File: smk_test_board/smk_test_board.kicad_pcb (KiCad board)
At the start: 2 copper layers, 76 x 113.2 mm, 46 parts, among them J1 Battery JST-SH, SW00 KS-2P02B01-02, SW01 KS-2P02B01-02, SW10 KS-2P02B01-02, SW11 KS-2P02B01-02, SW12 KS-2P02B01-02, SW20 KS-2P02B01-02, SW21 KS-2P02B01-02, SW22 KS-2P02B01-02, U1 XIAO_ESP32C6, U2 SN74AHCT1G125DBVR

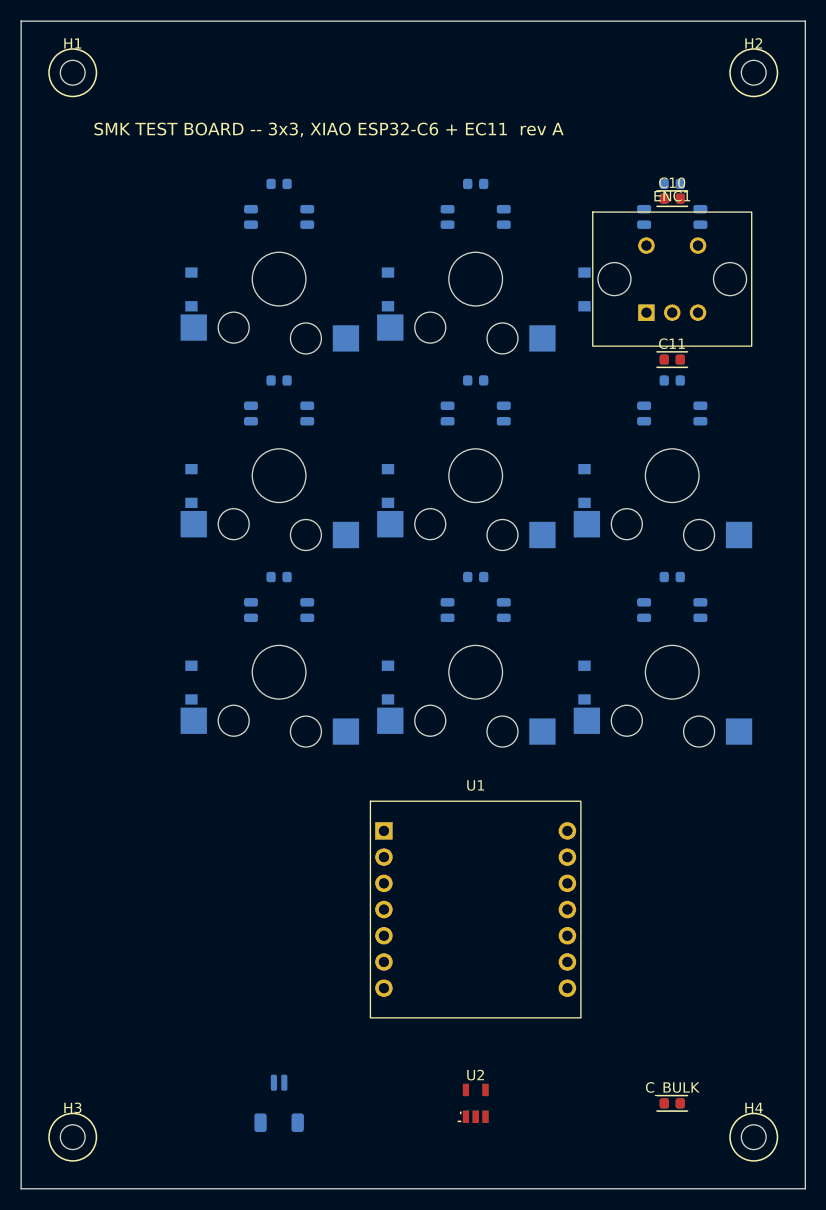
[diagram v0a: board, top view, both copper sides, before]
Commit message: Mill the SK6812MINI-E light windows into all nine LEDs
_fp_sk6812mini_tb() re-rendered the SK6812MINI-E footprint inline and
emitted 4 pads, 5 B.SilkS lines, a B.CrtYd rect, 2 B.Fab items and the
3D model -- then stopped. The library master
smk_test_board.pretty/SK6812MINI_E.kicad_mod additionally carries 20
Edge.Cuts primitives (8 fp_line + 12 fp_arc) forming the ~3.4 x 3.0mm
rounded-rect cutout, plus the pin-1 silk polarity triangle. None of that
was emitted.

These are REVERSE-MOUNT LEDs on the back of the board, shining forward
through it into each switch's north window. With no milled openings they
do nothing at all, and it cannot be reworked after fabrication.

  grep -c Edge.Cuts  smk_test_board/smk_test_board.kicad_pcb : 2  ->  182
  (1 layer declaration + 1 board outline + 9 LEDs x 20 primitives)
  Library master: 20. Proven sibling smk_kbd_rp2040 (58 LEDs): 1182.

The geometry is transcribed from the library master, not re-derived, and
cross-checked against how the sibling board actually stores its own 58
SK6812MINI_E instances: identical local numbers, footprint (at ... 180).
Footprint graphics live in footprint-LOCAL coordinates in both .kicad_mod
and .kicad_pcb -- KiCad applies each instance's own (at x y rot) -- so one
local copy lands correctly rotated at all nine placed positions.

The comment above these re-renders claimed they matched the library
master "byte-for-byte". They never did (the masters spell rectangles as
four fp_lines where gm.fprect() emits one fp_rect, and every uuid
differs), and that unfalsifiable-sounding claim is what let a dropped
layer survive review. Replaced with what is actually guaranteed --
equivalent geometry, per element-class -- and made checkable:

  test_inline_rerenders_match_their_library_master compares every inline
  re-render against its master by element-class (pads / silk / courtyard /
  fab / Edge.Cuts / text / model), normalising only the differences that
  are genuinely spelling and not geometry (fp_rect vs 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
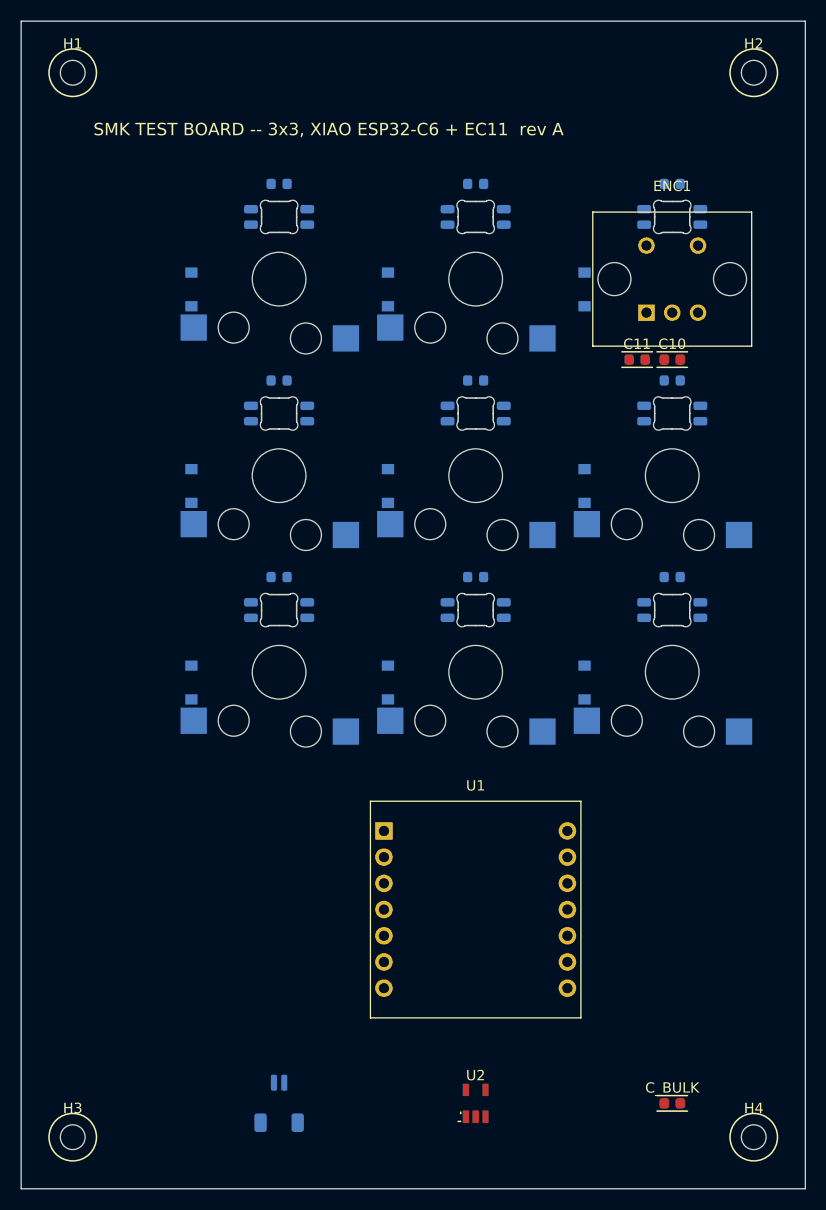
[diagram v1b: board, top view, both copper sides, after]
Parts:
- moved C10 15.6 mm to (63.1, 32.8)
- moved C11 3.40 mm to (59.7, 32.8)

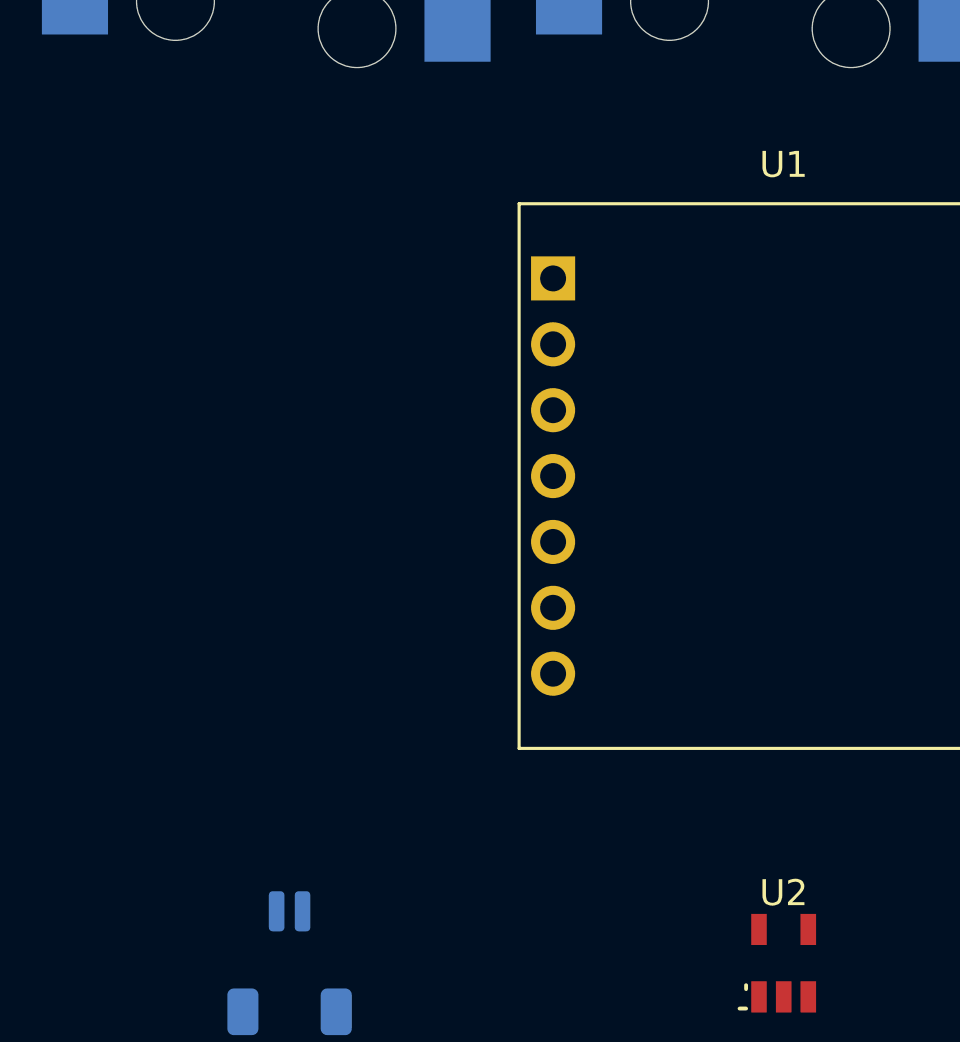
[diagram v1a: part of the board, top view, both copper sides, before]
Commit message: Wire the battery to the XIAO, add the VBAT divider, complete the schematic
Three defects with one shape: parts that build_nets()/build_pcb() should
have carried and didn't, or carried and never told the schematic about.

1. The battery never reached the XIAO.
   J1 (the JST cell connector) fed VSYS, and VSYS fed the nine SK6812 VDD
   pins, C1-C9, C_BULK and U2's VCC -- but nothing tied VSYS to U1. The
   board could not run untethered, the XIAO's onboard charger was never in
   circuit with the cell, and on USB with no cell fitted the whole LED
   chain and the level shifter were unpowered.

   The XIAO's BAT+/BAT- are solder pads on the module's UNDERSIDE and it
   seats on female headers, so no PCB pad can mate with them:
   XIAO_ESP32C6_HEADERS is 14 pads with no BAT pad, and that is correct.
   Added J2, a labelled 2-pin THROUGH-HOLE pad pair beside U1 for two
   short flying leads the user solders to the module's underside pads.

   THT, not SMD -- these take hand-soldered wire and an SMD pad tears off.
   Polarity is made unmistakable four ways (a reversed lead puts a Li-ion
   cell backwards into the XIAO): pad 1 is the square pin-1 pad, both pads
   carry "BAT+"/"BAT-" silk, a drawn silk "+" sits outboard of pad 1 and a
   drawn "-" outboard of pad 2.

   Placement is searched, not hand-picked: _placed_obstacles() reads every
   already-placed footprint's real courtyard out of gm.FPBOX in absolute
   board coordinates, and the search demands 1.5mm of clearance -- U1's
   courtyard is larger than the module's own 21 x 17.5mm body, so clearing
   it by 1.5mm is 1.5mm of open board beyond the seated module, enough for
   an iron tip and a wire. An assert refuses to place J2 without it. Board
   outline is unchanged at 76.0 x 113.16mm.

2. VBAT sense was unwired, and the spec's premise for that was wrong.
   PIN["VBAT_SENSE"] existed and drew a schematic port, but build_nets()
   referenced it zero times -- U1 pad 1 floated while firmware read
   ADC1_CH0 as a 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
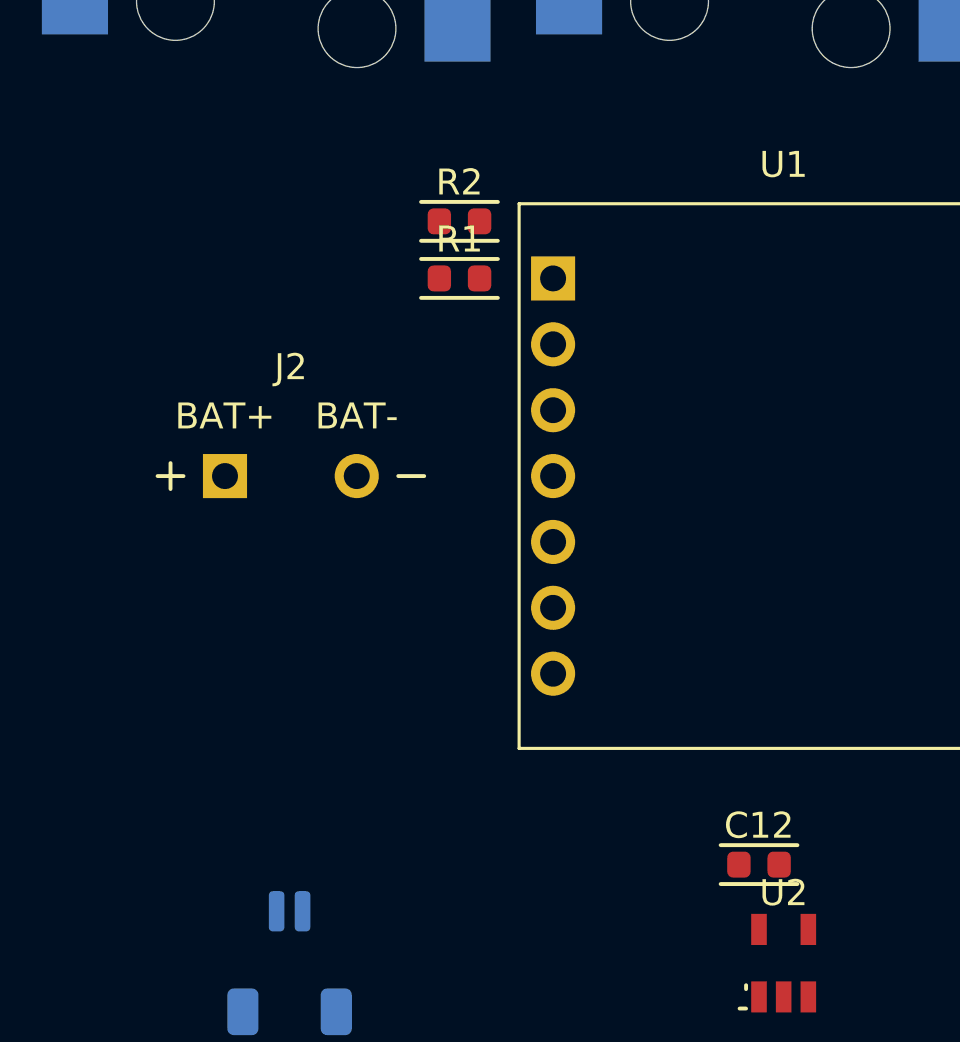
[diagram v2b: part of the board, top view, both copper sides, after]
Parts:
- added C12: 100n, kbd:RC_0603, F.Cu at (43.1, 101.1)
- added J2: BAT+ / BAT- flying leads, smk_test_board:BAT_WIRE_PADS, F.Cu at (25.1, 86.1)
- added R1: 200k, kbd:RC_0603, F.Cu at (31.6, 78.5)
- added R2: 200k, kbd:RC_0603, F.Cu at (31.6, 76.3)
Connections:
- U1 pad 1: (no net) -> VBAT_SENSE
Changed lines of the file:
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@@
   (net 28 "ENC_B")
   (net 29 "SW02_N")
+  (net 30 "VBAT_SENSE")
   (footprint "kbd:D_SOD-123_Back" (layer "B.Cu")
   (at 16.5 26 270)
@@
     (fp_line (start 10.2 10.5) (end -10.2 10.5) (stroke (width 0.12) (type solid)) (layer "F.SilkS"))
     (fp_line (start -10.2 10.5) (end -10.2 -10.5) (stroke (width 0.12) (type solid)) (layer "F.SilkS"))
-    (pad "1" thru_hole rect (at -8.89 -7.62) (size 1.7 1.7) (drill 1.0) (layers "*.Cu" "*.Mask"))
+    (pad "1" thru_hole rect (at -8.89 -7.62) (size 1.7 1.7) (drill 1.0) (layers "*.Cu" "*.Mask") (net 30 "VBAT_SENSE"))
     (pad "2" thru_hole circle (at -8.89 -5.08) (size 1.7 1.7) (drill 1.0) (layers "*.Cu" "*.Mask") (net 1 "ROW0"))
     (pad "3" thru_hole circle (at -8.89 -2.54) (size 1.7 1.7) (drill 1.0) (layers "*.Cu" "*.Mask") (net 2 "ROW1"))
@@
     (pad "14" thru_hole circle (at 8.89 7.62) (size 1.7 1.7) (drill 1.0) (layers "*.Cu" "*.Mask"))
   )
+  (footprint "smk_test_board:BAT_WIRE_PADS" (layer "F.Cu")
+  (at 25.05 86.1)
+  (property "Reference" "J2" (at 0 -4.2 0) (layer "F.SilkS")
+    (effects (font (size 1 1) (thickness 0.15)))
+  )
+  (property "Value" "BAT+ / BAT- flying leads" (at 0 4.2 0) (layer "F.Fab")
+    (effects (font (size 1 1) (thickness 0.15)))
+  )
+  (property "Footprint" "smk_test_board:BAT_WIRE_PADS" (at 0 0 0) (layer "F.Fab") (hide yes)
+    (effects (font (size 1.27 1.27))))
+  (property "Datasheet" "" (at 0 0 0) (layer "F.Fab") (hide yes)
+    (effects (font (size 1.27 1.27))))
+  (property "Description" "" (at 0 0 0) (layer "F.Fab") (hide yes)
+    (effects (font (size 1.27 1.27))))
+  (attr through_hole)
+    (pad "1" thru_hole rect (at -2.54 0) (size 1.7 1.7) (drill 1.0) (layers "*.Cu" "*.Mask") (net 18 "VSYS"))
+    (pad "2" thru_hole circle (at 2.54 0) (size 1.7 1.7) (drill 1.0) (layers "*.Cu" "*.Mask") (net 16 "GND"))
+    (fp_text user "BAT+" (at -2.54 -2.3) (layer "F.SilkS")
+      (effects (font (size 1 1) (thickness 0.15)))
+    )
+    (fp_text user "BAT-" (at 2.54 -2.3) (layer "F.SilkS")
+      (effects (font (size 1 1) (thickness 0.15)))
+    )
+    (fp_line (start -5.14 0) (end -4.14 0) (stroke (width 0.15) (type solid)) (layer "F.SilkS"))
+    (fp_line (start -4.64 -0.5) (end -4.64 0.5) (stroke (width 0.15) (type solid)) (layer "F.SilkS"))
+    (fp_line (start 4.14 0) (end 5.14 0) (stroke (width 0.15) (type solid)) (layer "F.SilkS"))
+    (fp_rect (start -3.4 -1) (end 3.4 1) (stroke (width 0.1) (type solid)) (fill none) (layer "F.Fab"))
+    (fp_rect (start -5.4 -3) (end 5.4 3) (stroke (width 0.05) (type solid)) (fill none) (layer "F.CrtYd"))
+  )
+  (footprint "kbd:RC_0603" (layer "F.Cu")
+  (at 31.55 78.48)
+  (property "Reference" "R1" (at 0 -1.5 0) (layer "F.SilkS")
+    (effects (font (size 1 1) (thickness 0.15)))
+  )
+  (property "Value" "200k" (at 0 1.5 0) (layer "F.Fab")
+    (effects (font (size 1 1) (thickness 0.15)))
+  )
+  (property "Footprint" "kbd:RC_0603" (at 0 0 0) (layer "F.Fab") (hide yes)
+    (effects (font (size 1.27 1.27))))
+  (property "Datasheet" "" (at 0 0 0) (layer "F.Fab") (hide yes)
+    (effects (font (size 1.27 1.27))))
+  (property "Description" "" (at 0 0 0) (layer "F.Fab") (hide yes)
+    (effects (font (size 1.27 1.27))))
+  (attr smd)
+    (pad "1" smd roundrect (at -0.775 0) (size 0.9 1) (layers "F.Cu" "F.Paste" "F.Mask") (net 18 "VSYS") (roundrect_rratio 0.25))
+    (pad "2" smd roundrect (at 0.775 0) (size 0.9 1) (layers "F.Cu" "F.Paste" "F.Mask") (net 30 "VBAT_SENSE") (roundrect_rratio 0.25))
+    (fp_rect (start -0.8 -0.4) (end 0.8 0.4) (stroke (width 0.1) (type solid)) (fill none) (layer "F.Fab"))
+    (fp_line (start -1.48 -0.75) (end 1.48 -0.75) (stroke (width 0.15) (type solid)) (layer "F.SilkS"))
+    (fp_line (start -1.48 0.75) (end 1.48 0.75) (stroke (width 0.15) (type solid)) (layer "F.SilkS"))
+    (fp_rect (start -1.5 -0.9) (end 1.5 0.9) (stroke (width 0.05) (type solid)) (fill none) (layer "F.CrtYd"))
+    (model "/Applications/KiCad/KiCad.app/Contents/SharedSupport/3dmodels/Resistor_SMD.3dshapes/R_0603_1608Metric.step"
+      (offset (xyz 0 0 0))
+      (scale (xyz 1 1 1))
+      (rotate (xyz 0 0 0))
+    )
+  )
+  (footprint "kbd:RC_0603" (layer "F.Cu")
+  (at 31.55 76.28)
+  (property "Reference" "R2" (at 0 -1.5 0) (layer "F.SilkS")
+    (effects (font (size 1 1) (thickness 0.15)))
+  )
+  (property "Value" "200k" (at 0 1.5 0) (layer "F.Fab")
+    (effects (font (size 1 1) (thickness 0.15)))
+  )
+  (property "Footprint" "kbd:RC_0603" (at 0 0 0) (layer "F.Fab") (hide yes)
+    (effects (font (size 1.27 1.27))))
+  (property "Datasheet" "" (at 0 0 0) (layer "F.Fab") (hide yes)
+    (effects (font (size 1.27 1.27))))
+  (property "Description" "" (at 0 0 0) (layer "F.Fab") (hide yes)
+    (effects (font (size 1.27 1.27))))
+  (attr smd)
+    (pad "1" smd roundrect (at -0.775 0) (size 0.9 1) (layers "F.Cu" "F.Paste" "F.Mask") (net 30 "VBAT_SENSE") (roundrect_rratio 0.25))
+    (pad "2" smd roundrect (at 0.775 0) (size 0.9 1) (layers "F.Cu" "F.Paste" "F.Mask") (net 16 "GND") (roundrect_rratio 0.25))
+    (fp_rect (start -0.8 -0.4) (end 0.8 0.4) (stroke (width 0.1) (type solid)) (fill none) (layer "F.Fab"))
+    (fp_line (start -1.48 -0.75) (end 1.48 -0.75) (stroke (width 0.15) (type solid)) (layer "F.SilkS"))
+    (fp_line (start -1.48 0.75) (end 1.48 0.75) (stroke (width 0.15) (type solid)) (layer "F.SilkS"))
+    (fp_rect (start -1.5 -0.9) (end 1.5 0.9) (stroke (width 0.05) (type solid)) (fill none) (layer "F.CrtYd"))
+    (model "/Applications/KiCad/KiCad.app/Contents/SharedSupport/3dmodels/Resistor_SMD.3dshapes/R_0603_1608Metric.step"
+      (offset (xyz 0 0 0))
+      (scale (xyz 1 1 1))
+      (rotate (xyz 0 0 0))
+    )
+  )
   (footprint "kbd:JST_SH_SM02B_2pin_Back" (layer "B.Cu")
   (at 25 104.88)
@@
       (offset (xyz 0 0 0))
       (scale (xyz 1 1 1))
+      (rotate (xyz 0 0 0))
+    )
+  )
+  (footprint "kbd:RC_0603" (layer "F.Cu")
+  (at 43.1 101.08)
+  (property "Reference" "C12" (at 0 -1.5 0) (layer "F.SilkS")
+    (effects (font (size 1 1) (thickness 0.15)))
+  )
+  (property "Value" "100n" (at 0 1.5 0) (layer "F.Fab")
+    (effects (font (size 1 1) (thickness 0.15)))
+  )
+  (property "Footprint" "kbd:RC_0603" (at 0 0 0) (layer "F.Fab") (hide yes)
+    (effects (font (size 1.27 1.27))))
+  (property "Datasheet" "" (at 0 0 0) (layer "F.Fab") (hide yes)
+    (effects (font (size 1.27 1.27))))
+  (property "Description" "" (at 0 0 0) (layer "F.Fab") (hide yes)
+    (effects (font (size 1.27 1.27))))
+  (attr smd)
+    (pad "1" smd roundrect (at -0.775 0) (size 0.9 1) (layers "F.Cu" "F.Paste" "F.Mask") (net 18 "VSYS") (roundrect_rratio 0.25))
+    (pad "2" smd roundrect (at 0.775 0) (size 0.9 1) (layers "F.Cu" "F.Paste" "F.Mask") (net 16 "GND") (roundrect_rratio 0.25))
+    (fp_rect (start -0.8 -0.4) (end 0.8 0.4) (stroke (width 0.1) (type solid)) (fill none) (layer "F.Fab"))
+    (fp_line (start -1.48 -0.75) (end 1.48 -0.75) (stroke (width 0.15) (type solid)) (layer "F.SilkS"))
+    (fp_line (start -1.48 0.75) (end 1.48 0.75) (stroke (width 0.15) (type solid)) (layer "F.SilkS"))
+    (fp_rect (start -1.5 -0.9) (end 1.5 0.9) (stroke (width 0.05) (type solid)) (fill none) (layer "F.CrtYd"))
+    (model "/Applications/KiCad/KiCad.app/Contents/SharedSupport/3dmodels/Resistor_SMD.3dshapes/R_0603_1608Metric.step"
+      (offset (xyz 0 0 0))
+      (scale (xyz 1 1 1))
